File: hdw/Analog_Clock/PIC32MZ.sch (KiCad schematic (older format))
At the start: 3 parts, among them U1001 PIC32MZ0512EFE064T-I_PT

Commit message: Much more schematic progress
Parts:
- R1001, R1002: Digi-Key PN (none) -> YAG2321CT-ND
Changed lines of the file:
@@
 encoding utf-8
 Sheet 10 25
-Title "Pulse Oximeter"
-Date "2020-08-01"
+Title "Analog Clock"
+Date "2020-08-15"
 Rev "A"
 Comp "Drew Maatman"
@@
 F 5 "1%" H 9430 2550 50  0000 L CNN "Tolerance"
 F 6 "1/10W" H 9440 2470 50  0000 L CNN "Wattage"
-F 7 "" H 9330 2550 50  0001 C CNN "Digi-Key PN"
+F 7 "YAG2321CT-ND" H 9330 2550 50  0001 C CNN "Digi-Key PN"
 	1    9330 2550
 	1    0    0    -1
@@
 F 5 "1%" H 8840 2550 50  0000 L CNN "Tolerance"
 F 6 "1/10W" H 8850 2470 50  0000 L CNN "Wattage"
-F 7 "" H 8740 2550 50  0001 C CNN "Digi-Key PN"
+F 7 "YAG2321CT-ND" H 8740 2550 50  0001 C CNN "Digi-Key PN"
 	1    8740 2550
 	1    0    0    -1

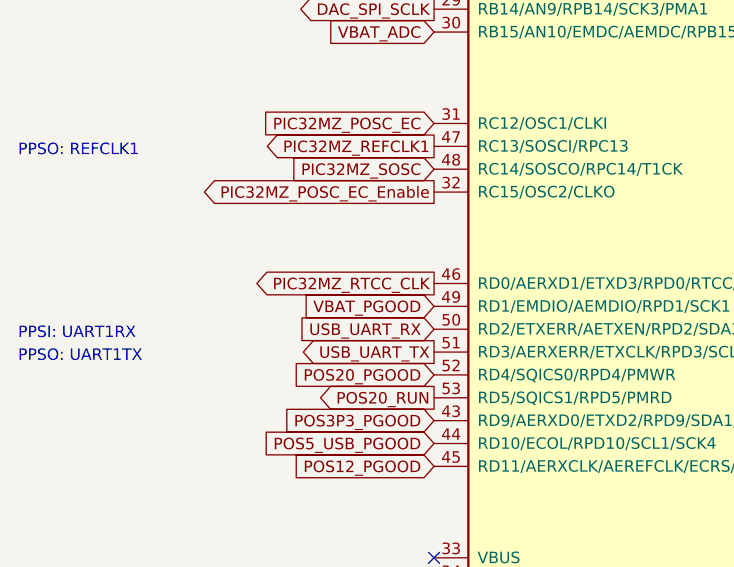
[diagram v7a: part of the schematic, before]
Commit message: Arranged more components on PCB
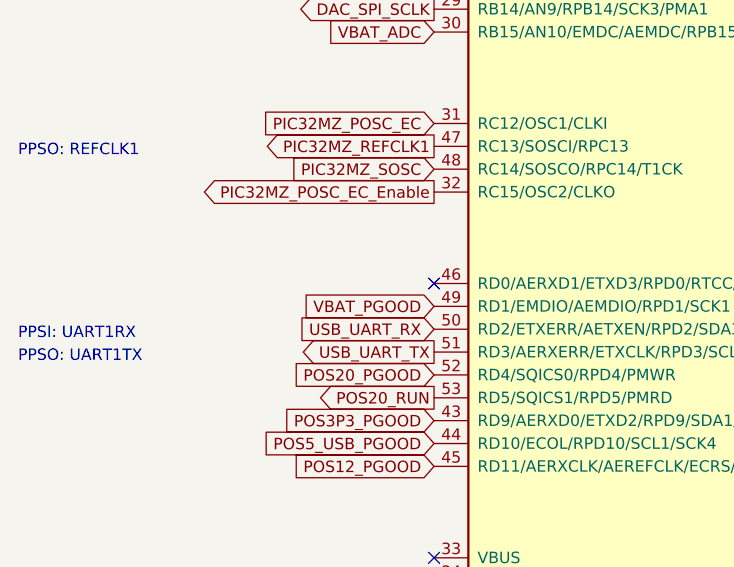
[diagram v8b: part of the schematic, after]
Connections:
- net PIC32MZ_RTCC_CLK: no longer names the net of U1001.46 (RD0/AERXD1/ETXD3/RPD0/RTCC/INT0)
- no-connect marks 5 -> 6
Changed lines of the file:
@@
 Text Notes 1500 2370 0    50   ~ 0
 ICSP2
-Text GLabel 3320 4280 0    50   Output ~ 0
-PIC32MZ_RTCC_CLK
 Text GLabel 7520 2580 2    50   Output ~ 0
 Meter_LED_Enable
@@
 Text GLabel 7520 1880 2    50   Output ~ 0
 Buzzer_Enable
+NoConn ~ 3320 4280
 $EndSCHEMATC
